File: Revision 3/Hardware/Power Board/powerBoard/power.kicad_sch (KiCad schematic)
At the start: 14 parts, among them J1 1366005, J7 Conn_01x02, SW1 SW_SPST

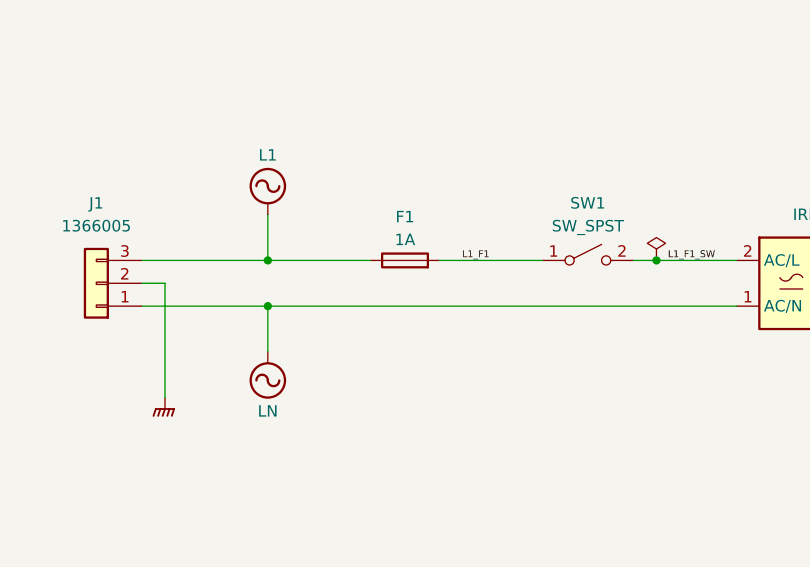
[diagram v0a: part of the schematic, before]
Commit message: Change AC-DC supply fuse holder part number, ordered the wrong one
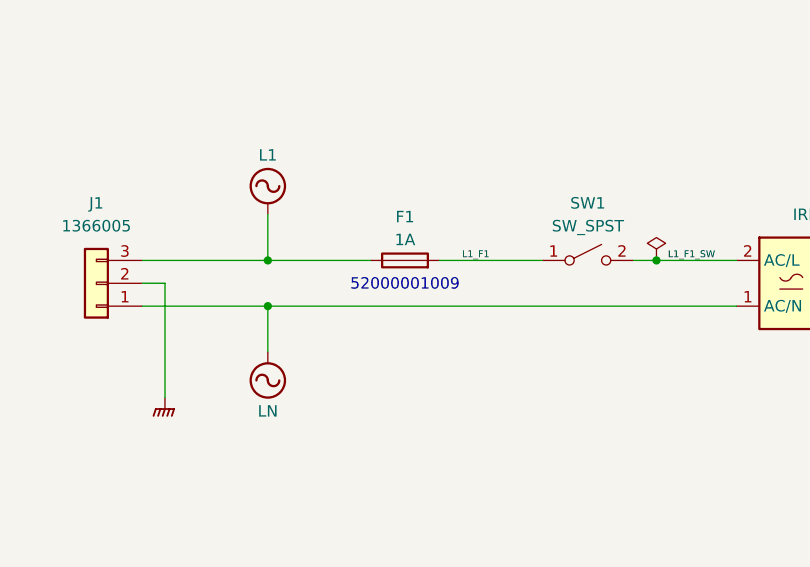
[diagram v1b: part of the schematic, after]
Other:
- note added: "52000001009"
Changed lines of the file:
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@@
 		(company "${COMPANY}")
+	)
+	(text "52000001009"
+		(exclude_from_sim no)
+		(at 165.1 189.484 0)
+		(effects
+			(font
+				(size 1.27 1.27)
+			)
+		)
 	)
 	(text_box "IRM-10-5\n5VDC Output\n10W Power\nVDD = 5V"
